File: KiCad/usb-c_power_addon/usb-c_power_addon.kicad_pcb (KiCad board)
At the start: 4 copper layers, 72.8 x 82.1 mm, 76 parts, among them IC1 AP63205, IC2 AP2112K-3.3TRG1, J1 GT-USB-7025, J10 10PIN_HEADER, J11 10PIN_HEADER, J15 12PIN_SERVO_HEADER, J2 Conn_Coaxial, J3 1987724, J4 1987724, J5 1987724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

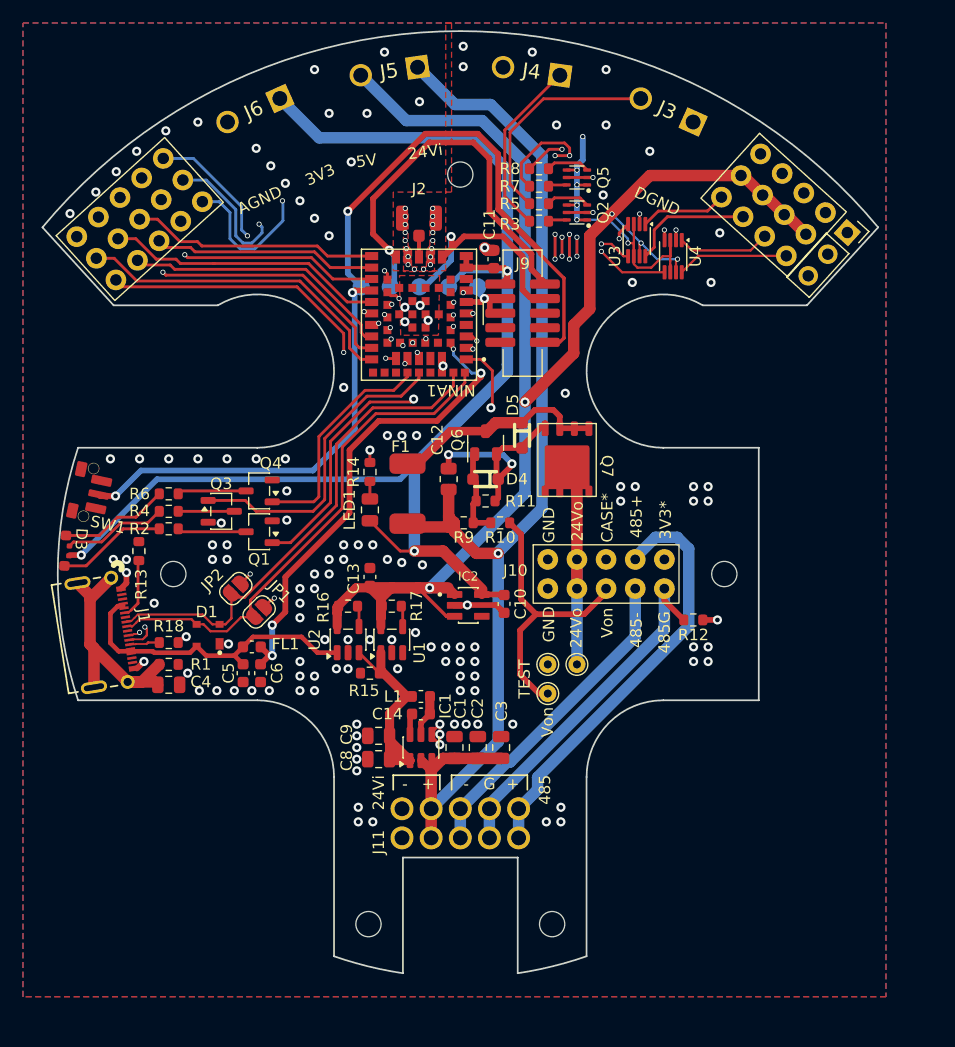
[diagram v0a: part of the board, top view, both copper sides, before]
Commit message: finished usb-c power addon, fixed main usbc wonky traces
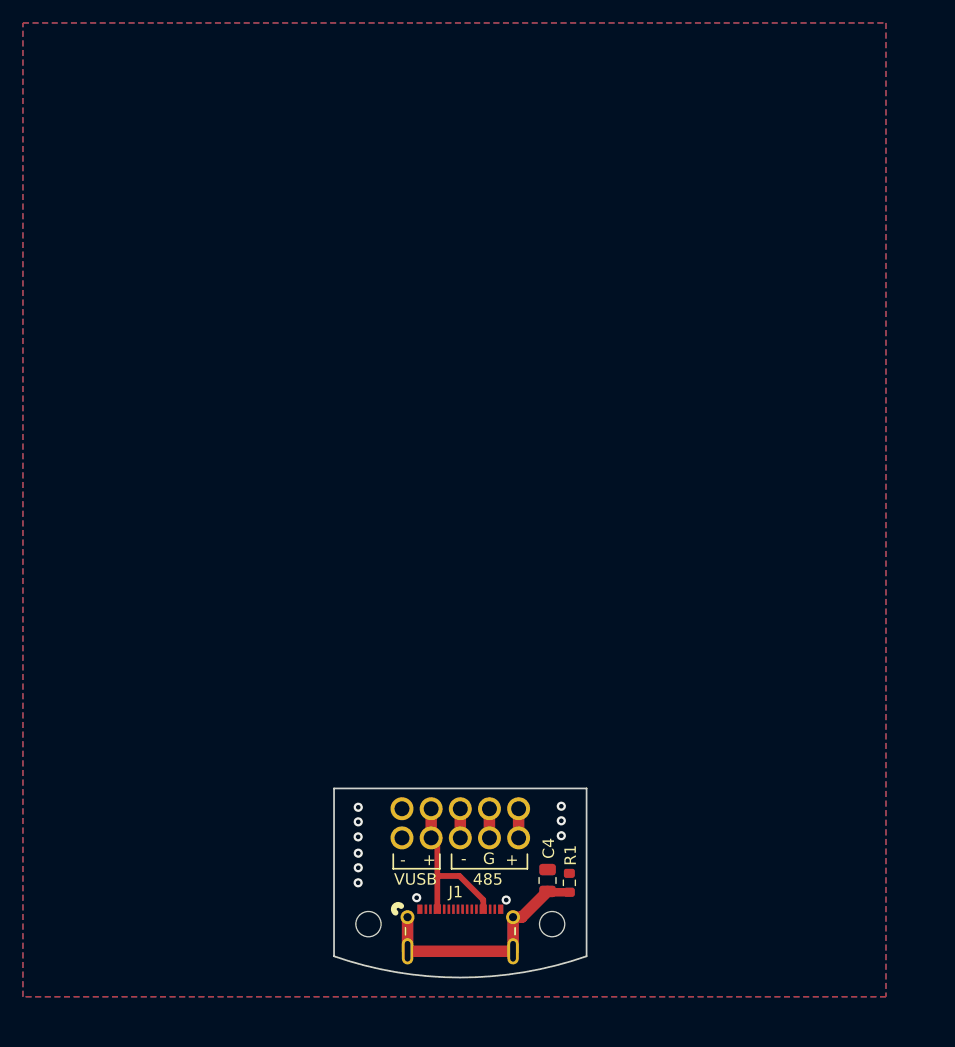
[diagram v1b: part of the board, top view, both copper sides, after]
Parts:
- removed C1, C2, C3, C8, C9: 22µF, Capacitor_SMD:C_0805_2012Metric
- removed C10: 1µF, Capacitor_SMD:C_0603_1608Metric
- removed C11, C14: 100nF, Capacitor_SMD:C_0603_1608Metric
- removed C12: 15u, Resistor_SMD:R_0805_2012Metric
- removed C13: 4µ7 (1mOhm ESR), Capacitor_SMD:C_0603_1608Metric
- removed C5, C6: 1n, Capacitor_SMD:C_0603_1608Metric
- removed D1: PRTR5V0U2AX,215, robotiq_wrist_coupling:SOT143B
- removed D3: LED_RGBA, robotiq_wrist_coupling:XZCCBDMEDGK161W
- removed D4, D5: DIODE, robotiq_wrist_coupling:DO-219AC
- removed F1: LF110-33, robotiq_wrist_coupling:1812L110-33
- removed FL1: BLM18EG101TN1D, Capacitor_SMD:C_0603_1608Metric
- removed IC1: AP63205, Package_TO_SOT_SMD:TSOT-23-6
- removed IC2: AP2112K-3.3TRG1, robotiq_wrist_coupling:SOT95P285X140-5N
- removed J10: 10PIN_HEADER, robotiq_wrist_coupling:10PIN_SPRING_HEADER
- removed J15: 12PIN_SERVO_HEADER, robotiq_wrist_coupling:12PIN_SERVO_HEADER
- removed J2: Conn_Coaxial, robotiq_wrist_coupling:2337019-1 µCOAX
- removed J3, J4, J5, J6: 1987724, robotiq_wrist_coupling:1987724
- removed J7: 3PIN_HEADER, Connector_PinSocket_2.54mm:PinSocket_1x03_P2.54mm_Vertical
- removed J8: 15PIN_HEADER, robotiq_wrist_coupling:15PIN_HEADER
- removed J9: 10PIN_HEADER, robotiq_wrist_coupling:10PIN_1.27PITCH
- removed JP1, JP2: SolderJumper_2_Open, Jumper:SolderJumper-2_P1.3mm_Open_RoundedPad1.0x1.5mm
- removed L1: 4µ7, Inductor_SMD:L_0603_1608Metric
- removed LED1: LTST-C170GKT, Capacitor_SMD:C_0805_2012Metric
- removed NINA1: ~, robotiq_wrist_coupling:NINA-B301-00B
- removed Q1, Q3, Q4: BSS138K-13, Package_TO_SOT_SMD:SOT-23-3
- removed Q2, Q5: RN2903, robotiq_wrist_coupling:US6_RN2903
- removed Q6: BSS159NH6327XTSA2, robotiq_wrist_coupling:BSS138
- removed Q7: Si7469DP, robotiq_wrist_coupling:si7469dp
- removed R10: 50k, Resistor_SMD:R_0603_1608Metric
- removed R11, R9: 100k, Resistor_SMD:R_0603_1608Metric
- removed R12: 0, Resistor_SMD:R_0603_1608Metric
- removed R13, R18: 5.1k, Resistor_SMD:R_0603_1608Metric
- removed R14: 560, Resistor_SMD:R_0603_1608Metric
- removed R15, R16, R17: 470k, Resistor_SMD:R_0603_1608Metric
- removed R2, R6: 330, Resistor_SMD:R_0603_1608Metric
- removed R3, R5, R7, R8: 7k32, Resistor_SMD:R_0603_1608Metric
- removed R4: 750, Resistor_SMD:R_0603_1608Metric
- removed SW1: TL3340, robotiq_wrist_coupling:TL3340
- removed TP1, TP2, TP3, TP4, TP5: TestPoint, TestPoint:TestPoint_Pad_D1.5mm
- removed TP6, TP7, TP8: TestPoint, TestPoint:TestPoint_THTPad_D1.5mm_Drill0.7mm
- removed U1, U2: LTC4411ES5-TRMPBF, Package_TO_SOT_SMD:TSOT-23-5
- removed U3, U4: TXB0102DCU, Package_SO:VSSOP-8_2.3x2mm_P0.5mm
- moved J1 41.7 mm to (0.00, 32.1), turned to 0 degrees
- moved R1 39.7 mm to (9.50, 26.9), turned to 90 degrees
- moved C4 37.1 mm to (7.60, 26.7), turned to 90 degrees
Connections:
- J1 pad 10: Net-(J1-B7/D-) -> unconnected-(J1-B7/D--Pad10)
- J1 pad 11: Net-(J1-B6/D+) -> unconnected-(J1-B6/D+-Pad11)
- J1 pad 12: Net-(J1-B5/CC2) -> unconnected-(J1-B5/CC2-Pad12)
- J1 pad 5: Net-(J1-A5/CC1) -> unconnected-(J1-A5/CC1-Pad5)
- J1 pad 7: /USB_D+ -> unconnected-(J1-A6/D+-Pad7)
- J1 pad 8: /USB_D- -> unconnected-(J1-A7/D--Pad8)
- J11 pad 3: /24V_in -> /VBUS
- J11 pad 4: /24V_in -> /VBUS
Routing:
- net /3V3: track 164.9 -> 0.00 mm, vias 9 -> 0
- net /5V: track 133.3 -> 0.00 mm, vias 5 -> 0
- net /24V_in: track 101.7 -> 0.00 mm, vias 1 -> 0
- net /RESET: track 83.0 -> 0.00 mm, vias 3 -> 0
- net /SCL2/D6: track 59.2 -> 0.00 mm, vias 5 -> 0
- net /SDA2/D5: track 57.2 -> 0.00 mm, vias 4 -> 0
- net /SDA1/MISO/D16: track 49.3 -> 0.00 mm, vias 1 -> 0
- net /D4: track 47.9 -> 0.00 mm, vias 1 -> 0
- net /USB_D-: track 44.8 -> 0.00 mm
- net /USB_D+: track 43.5 -> 0.00 mm
- net /VBUS_filtered: track 42.0 -> 0.00 mm, vias 4 -> 0
- net /SCL1/MOSI/D15: track 41.4 -> 0.00 mm, vias 1 -> 0
- net /SWD: track 35.0 -> 0.00 mm, vias 1 -> 0
- net /RS485+: track 37.3 -> 2.54 mm
- net /D2: track 34.1 -> 0.00 mm, vias 2 -> 0
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- removed copper zone on In1.Cu, net GND
- removed copper zone on In2.Cu, net GND
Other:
- board size 72.8 x 82.1 mm -> 22 x 16.5 mm
- copper layers 4 -> 2
- board text added: "The main Halberd PCB is max. 6.1mm thick, including 1.6mm board thickness. This PCB is soldered on top, and the USBC port is 3.31mm thick -> for consistency, thickness of this board should be <1.19, i.e. 1mm, 0.8mm for more margin"
- board text added: "VUSB"
- board text removed: "24Vo"
- board text removed: "3V3"
- board text removed: "3V3*"
- board text removed: "5V"
- board text removed: "AGND"
- board text removed: "CASE*"
- board text removed: "DGND"
- board text removed: "Order Impedance Controlled JLC04161H-7628 (0.35mm ANT trace width corresponds to this)"
- board text removed: "RESET"
- board text removed: "SCK"
- board text removed: "SCL1 MOSI"
- board text removed: "SDA1 MISO"
- board text removed: "SWC"
- board text removed: "SWD"
- board text removed: "TEST"
- board text removed: "Von"
